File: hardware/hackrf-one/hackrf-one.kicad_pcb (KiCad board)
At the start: 4 copper layers, 120 x 75 mm, 431 parts, among them J1 USB-MICRO-B, J10 GND_CLIP, J2 RF-SHIELD-FRAME, J3 RF-SHIELD-COVER, J4 MOUNTING_HOLE, J5 MOUNTING_HOLE, J6 MOUNTING_HOLE, J7 MOUNTING_HOLE, J8 MOUNTING_HOLE, J9 MOUNTING_HOLE, P13 GPO1, P14 XCVR_CLKOUT, P15 INTR, P16 CLKIN, P17 GPO6, P18 OEB, P19 GPO3, P2 CLKOUT, P20 GPIO, P21 REF_IN, P22 I2S, P23 DBGEN, P24 TRST, P25 LPC_ISP, P26 LPC_JTAG, P27 MIXER_SDATA, P28 SD, P29 CPLD_JTAG, P3 GND, P30 BANK2_AUX, P31 MIXER_SCLK, P32 MIXER_ENX, P33 MIXER_RESETX, P34 MIX_BYPASS, P35 !MIX_BYPASS, P37 SCL, P38 SDA, P39 SSP1_SCK, P4 ANTENNA, P40 SSP1_COPI, P41 SSP1_CIPO, P43 RX, P44 HP, P45 LP, P46 TX_MIX_BP, P47 RX_MIX_BP, P48 TX_AMP, P49 RX_AMP, P5 LEDS, P50 AMP_BYPASS, P51 !TX_AMP_PWR, P52 !RX_AMP_PWR, P53 CS_XCVR, P54 CS_AD, P55 TXENABLE, P56 RXENABLE, P57 XTAL2, P58 GCK1, P59 GCK2, P6 GPO4, P60 SGPIO_CLK, P61 DA0, P62 DA7, P63 DD0, P64 DD9, P65 DA4, P66 DD5, P67 RSSI, P68 SPIFI_CS, P69 VREGMODE, P7 GPO2, P70 EN_1V8, P71 ID, P72 GP_CLKIN, P73 P1_2, P74 P1_1, P75 GP_CLKIN, P76 GP_CLKIN, P77 GP_CLKIN, P78 GP_CLKIN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

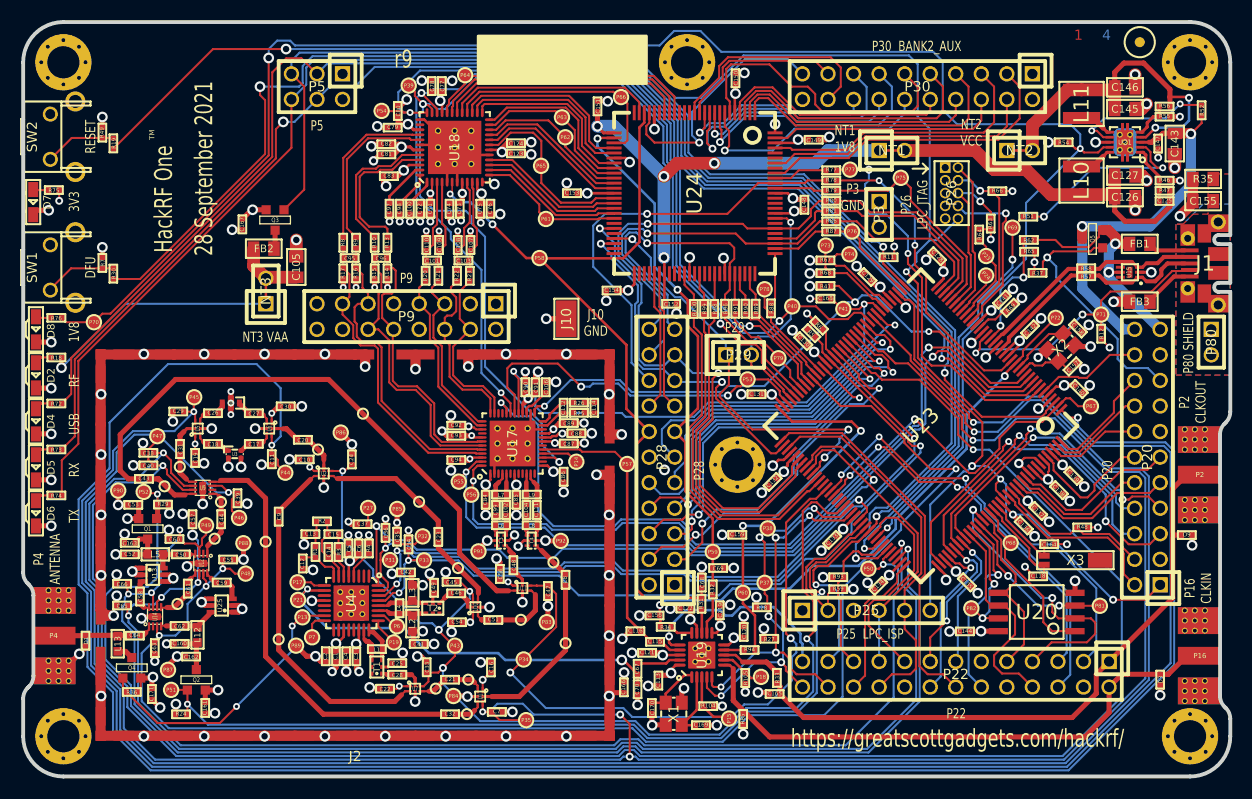
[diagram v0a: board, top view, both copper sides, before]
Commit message: HackRF One: update to KiCad 6
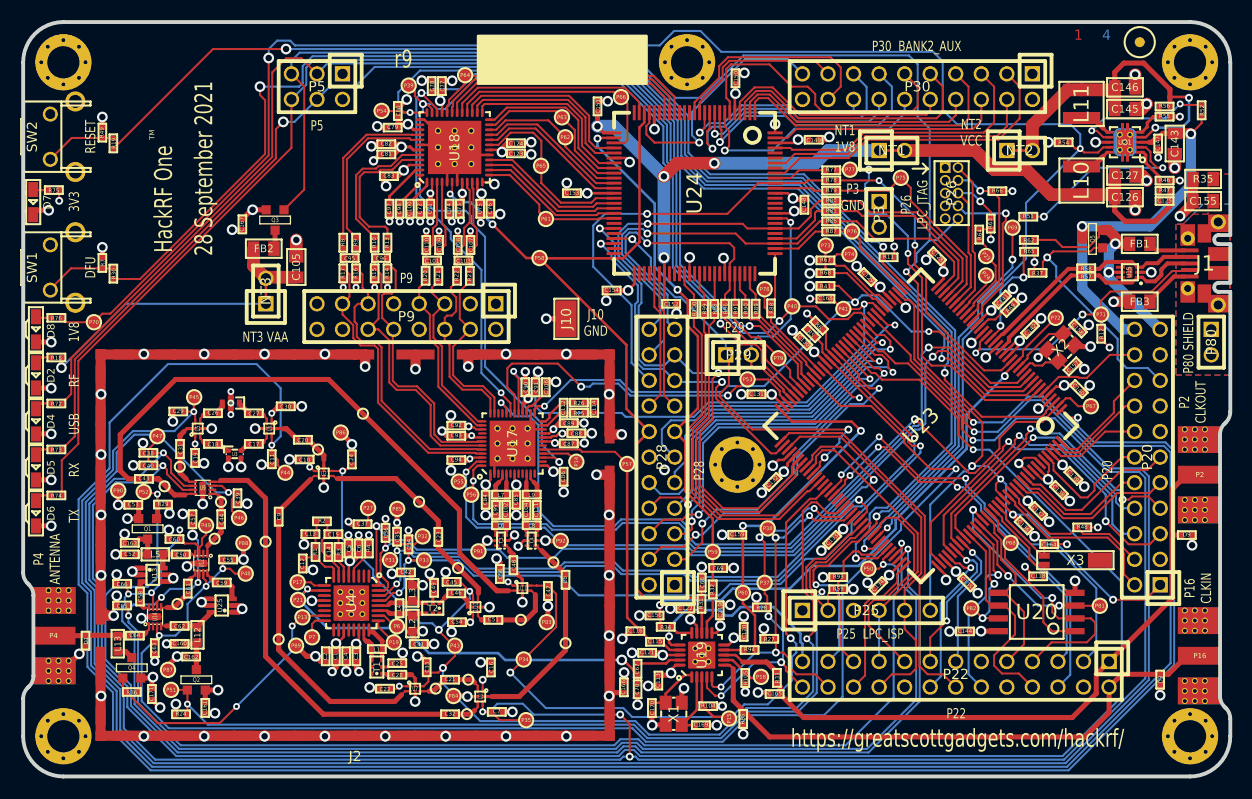
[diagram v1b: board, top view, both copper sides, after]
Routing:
- added copper zone on In1.Cu, net GND
- added copper zone on In2.Cu, net VAA
- added copper zone on In2.Cu, net VCC
- removed copper zone on C2, net GND
- removed copper zone on C3, net VAA
- removed copper zone on C3, net VCC
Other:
- net class Default removed

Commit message: HackRF One: update PCB stack-up specification
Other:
- rule pad_to_mask_clearance: 0.0762 -> 0.05
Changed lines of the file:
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@@
 (kicad_pcb (version 20211014) (generator pcbnew)
   (general
-    (thickness 1.6002)
+    (thickness 1.6116)
   )
   (paper "USLegal")
@@
     (41 "Cmts.User" user "User.Comments")
     (44 "Edge.Cuts" user)
+    (45 "Margin" user)
+    (46 "B.CrtYd" user "B.Courtyard")
+    (47 "F.CrtYd" user "F.Courtyard")
   )
   (setup
-    (pad_to_mask_clearance 0.0762)
+    (stackup
+      (layer "F.SilkS" (type "Top Silk Screen") (color "White"))
+      (layer "F.Paste" (type "Top Solder Paste"))
+      (layer "F.Mask" (type "Top Solder Mask") (color "Green") (thickness 0.0127) (material "LPI") (epsilon_r 3.8) (loss_tangent 0))
+      (layer "F.Cu" (type "copper") (thickness 0.035))
+      (layer "dielectric 1" (type "prepreg") (thickness 0.2104) (material "7628") (epsilon_r 4.6) (loss_tangent 0))
+      (layer "In1.Cu" (type "copper") (thickness 0.0152))
+      (layer "dielectric 2" (type "core") (thickness 1.065) (material "7628") (epsilon_r 4.6) (loss_tangent 0))
+      (layer "In2.Cu" (type "copper") (thickness 0.0152))
+      (layer "dielectric 3" (type "prepreg") (thickness 0.2104) (material "7628") (epsilon_r 4.6) (loss_tangent 0))
+      (layer "B.Cu" (type "copper") (thickness 0.035))
+      (layer "B.Mask" (type "Bottom Solder Mask") (color "Green") (thickness 0.0127) (material "LPI") (epsilon_r 3.8) (loss_tangent 0))
+      (layer "B.Paste" (type "Bottom Solder Paste"))
+      (layer "B.SilkS" (type "Bottom Silk Screen") (color "White"))
+      (copper_finish "ENIG")
+      (dielectric_constraints yes)
+    )
+    (pad_to_mask_clearance 0.05)
     (pad_to_paste_clearance_ratio -0.12)
     (pcbplotparams
